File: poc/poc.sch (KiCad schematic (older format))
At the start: 47 parts

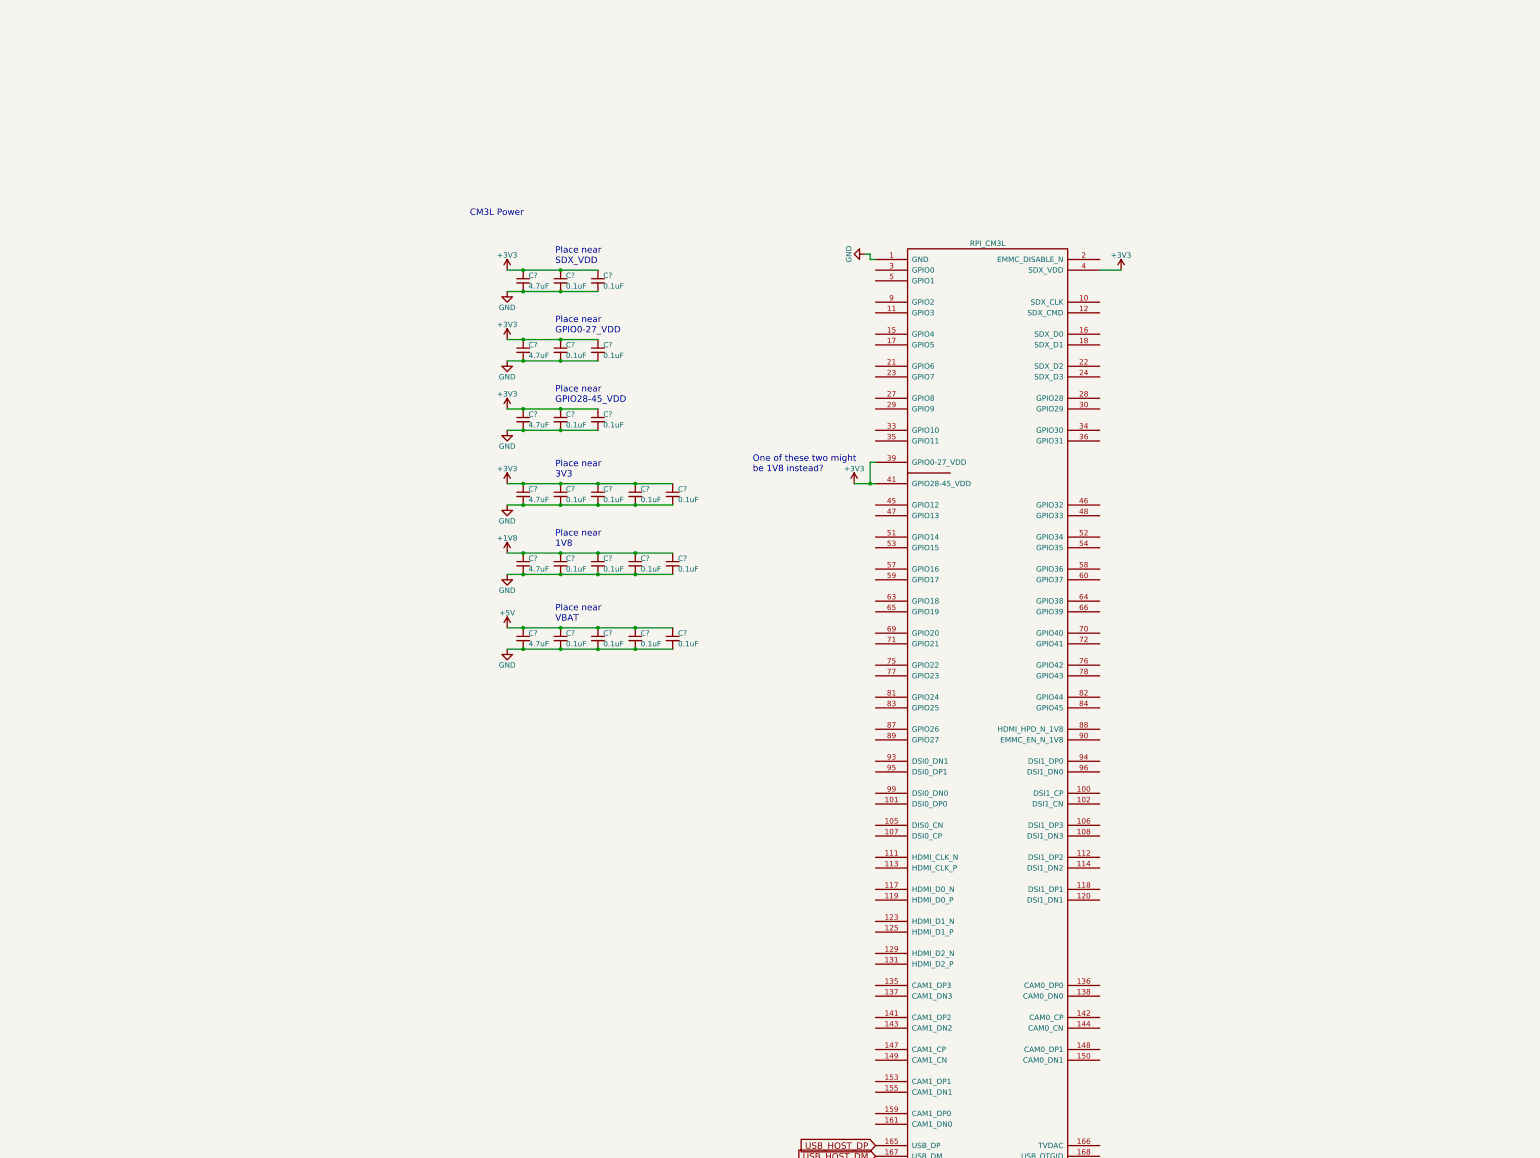
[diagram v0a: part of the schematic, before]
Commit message: Done with power layout for top cm3l
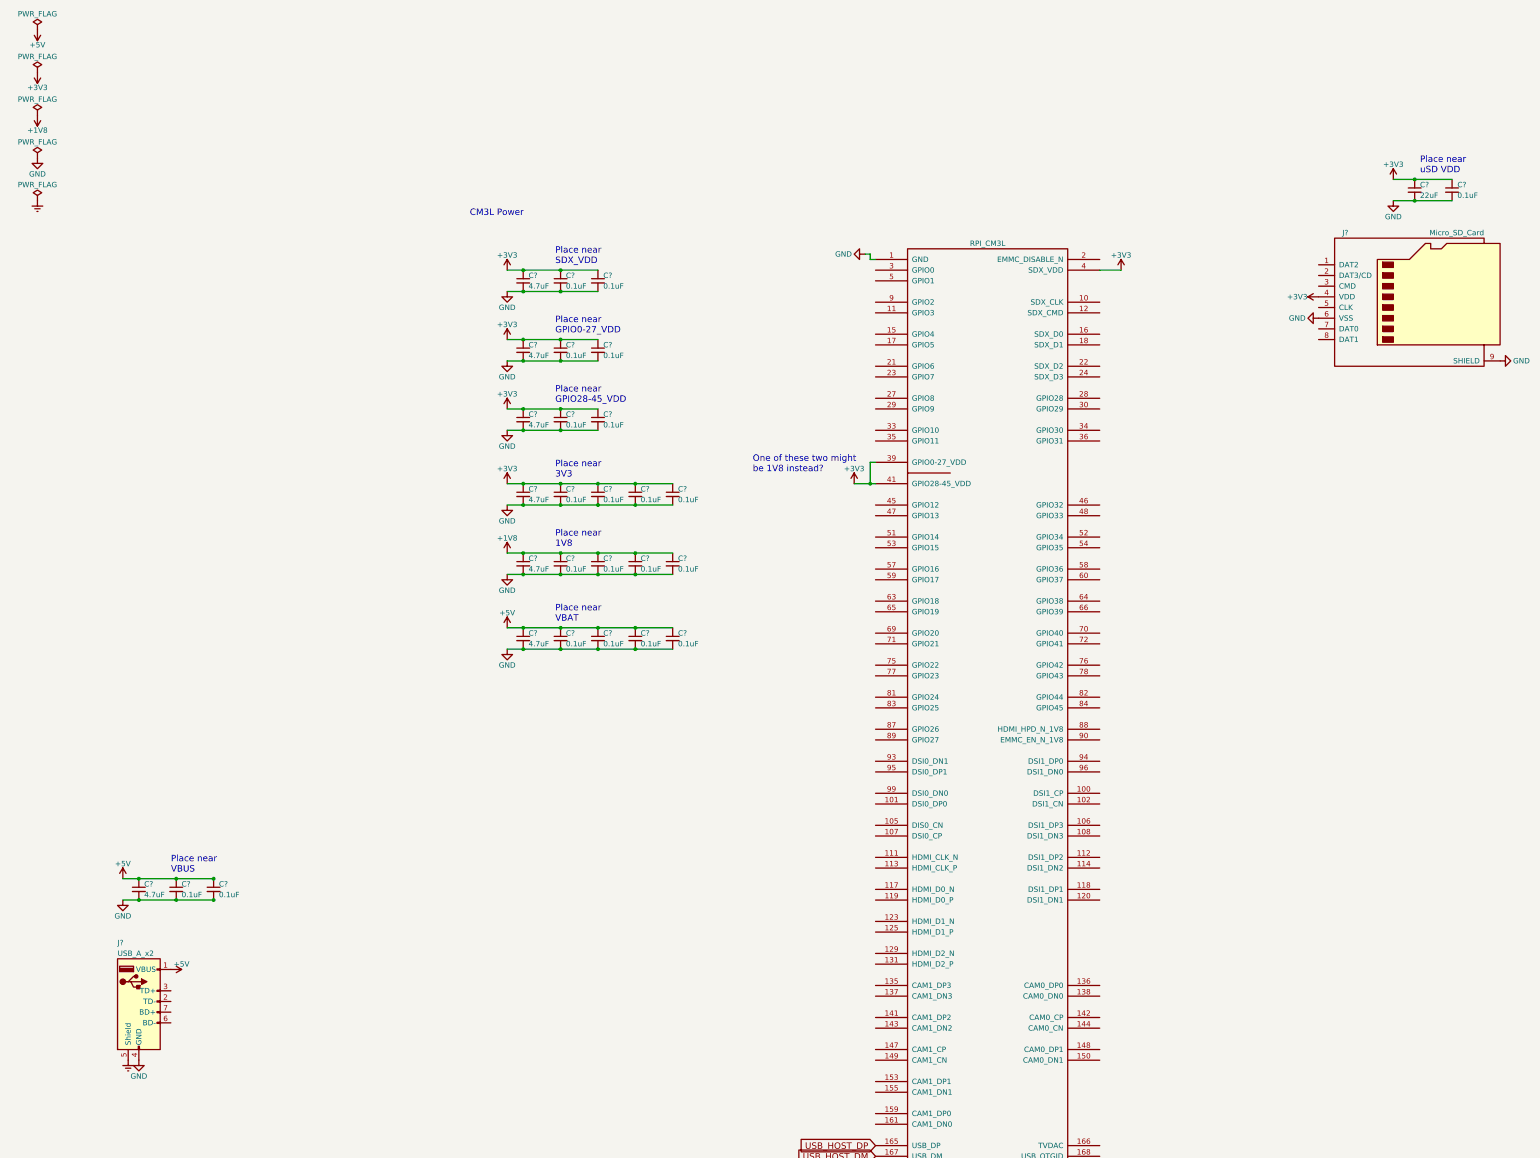
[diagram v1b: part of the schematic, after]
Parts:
- added C?: 4.7uF, symbol C_Small
- added C? (x3): 0.1uF, symbol C_Small
- added C?: 22uF, symbol C_Small
- added J?: USB_A_x2, symbol USB_A_x2
- added J?: Micro_SD_Card, symbol Micro_SD_Card
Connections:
- net +3V3: now also C?.1, C?.1, J?.4 (VDD)
- net +5V: now also C?.1, C?.1, C?.1, J?.1 (VBUS), J?.5 (VBUS)
- net GND: now also C?.2, C?.2, C?.2, C?.2, C?.2, J?.4 (GND), J?.6 (VSS), J?.8 (GND), J?.9 (SHIELD)
- new net Earth: J?.5 (VBUS)
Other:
- note added: "Place near\nVBUS"
- note added: "Place near\nuSD VDD"

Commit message: Move CM3L into hierarchical sheet
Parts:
- removed C? (x37): 0.1uF, symbol C_Small
- removed C? (x9): 4.7uF, symbol C_Small
- removed C?: 1.0uF, symbol C_Small
- removed C?: 22uF, symbol C_Small
- removed J?: USB_A_x2, symbol USB_A_x2
- removed J?: Micro_SD_Card, symbol Micro_SD_Card
- removed L? (x2): 120Ω @ 100MHz; 2.0A, symbol L_Core_Ferrite
- removed TopPi1: RPI_CM3L, symbol RPI_CM3L
- removed U?: LAN9512, MODULE, symbol LAN9512
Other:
- note removed: "CM3L Power"
- note removed: "Ferrite Bead"
- note removed: "LAN9512 Power"
- note removed: "One of these two might\nbe 1V8 instead?"
- note removed: "Place near\n1V8"
- note removed: "Place near\n3V3"
- note removed: "Place near\nGPIO0-27_VDD"
- note removed: "Place near\nGPIO28-45_VDD"
- note removed: "Place near\nSDX_VDD"
- note removed: "Place near\nVBAT"
- note removed: "Place near\nVBUS"
- note removed: "Place near\nVDD18CORE"
- note removed: "Place near\nVDD33A"
- note removed: "Place near\nVDD33IO"
- note removed: "Place near\nuSD VDD"

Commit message: Add one switch chip and power for things
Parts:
- added C? (x14): 0.1uF, symbol C_Small
- added C? (x2): 4.7uF, symbol C_Small
- added U?: SAM4E, MODULE, symbol SAM4E
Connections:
- net +3V3: now also C?.1, C?.1, C?.1, C?.1, C?.1, C?.1, C?.1, C?.1, U?.134 (VDDIO), U?.143 (VDDIO), U?.30 (VDDIO), U?.43 (VDDIO), U?.5 (VDDIN), U?.72 (VDDIO), U?.80 (VDDIO), U?.96 (VDDIO)
- net GND: now also C?.2, C?.2, C?.2, C?.2, C?.2, C?.2, C?.2, C?.2, C?.2, C?.2, C?.2, C?.2, C?.2, C?.2, C?.2, C?.2, U?.115 (GND), U?.135 (GND), U?.138 (GND), U?.44 (GND), U?.61 (GND), U?.8 (GND), U?.95 (GND)
- new net VDDCORE: C?.1, C?.1, C?.1, C?.1, C?.1, C?.1, C?.1, C?.1, U?.107 (VDDCORE), U?.123 (VDDCORE), U?.139 (VDDPLL), U?.29 (VDDCORE), U?.3 (VDDOUT), U?.33 (VDDCORE), U?.50 (VDDCORE), U?.81 (VDDCORE)
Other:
- note added: "Place near\nVDDCORE \n& VDDPLL"
- note added: "Place near\nVDDIO\n& VDDIN"

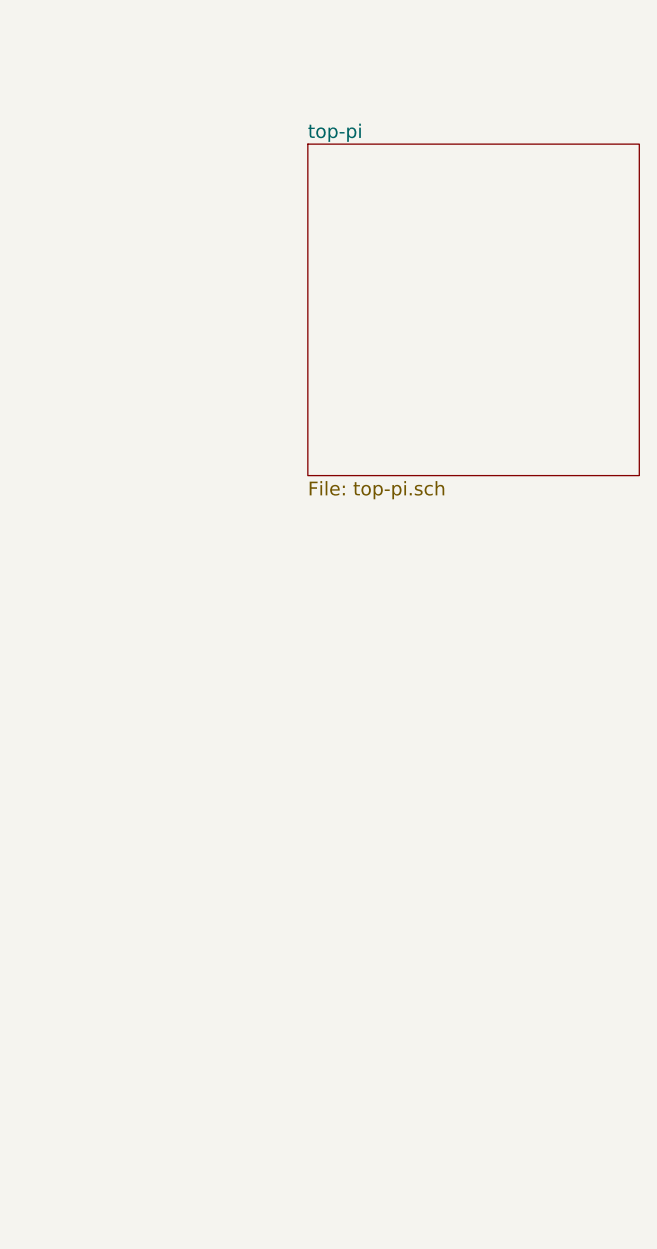
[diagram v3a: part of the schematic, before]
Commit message: Further organize pi schematics; power for each chip is done!
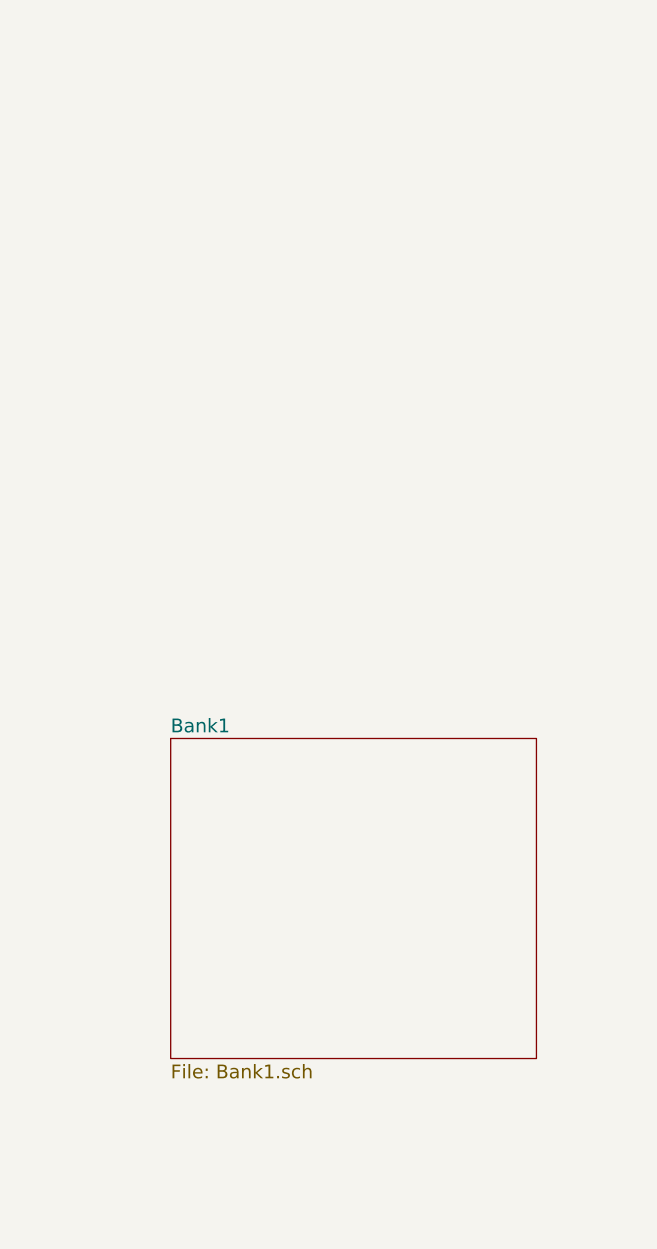
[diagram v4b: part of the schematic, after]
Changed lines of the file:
@@
 $Descr C 22000 17000
 encoding utf-8
-Sheet 1 3
+Sheet 1 4
 Title ""
 Date ""
@@
 	1    0    0    -1
 $EndComp
-$Sheet
-S 17850 1050 1450 1450
-U 598EEE5F
-F0 "top-pi" 60
-F1 "top-pi.sch" 60
-$EndSheet
 $Comp
 L SAM4E U?
@@
 F1 "switches.sch" 60
 $EndSheet
+$Sheet
+S 17250 3650 1600 1400
+U 5992D94E
+F0 "Bank1" 60
+F1 "Bank1.sch" 60
+$EndSheet
 $EndSCHEMATC

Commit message: Upgrade to newer kicad
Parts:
- C? (x16): symbol C_Small -> poc-rescue:C_Small
- U?: symbol SAM4E -> SAM4E:SAM4E
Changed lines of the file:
@@
-EESchema Schematic File Version 2
-LIBS:power
-LIBS:device
-LIBS:transistors
-LIBS:conn
-LIBS:linear
-LIBS:regul
-LIBS:74xx
-LIBS:cmos4000
-LIBS:adc-dac
-LIBS:memory
-LIBS:xilinx
-LIBS:microcontrollers
-LIBS:dsp
-LIBS:microchip
-LIBS:analog_switches
-LIBS:motorola
-LIBS:texas
-LIBS:intel
-LIBS:audio
-LIBS:interface
-LIBS:digital-audio
-LIBS:philips
-LIBS:display
-LIBS:cypress
-LIBS:siliconi
-LIBS:opto
-LIBS:atmel
-LIBS:contrib
-LIBS:valves
-LIBS:cm3l
-LIBS:LAN9512
-LIBS:usb_a_x2
-LIBS:CD74HC154
-LIBS:sc16is752
-LIBS:KSZ9897R
-LIBS:belfuse_gige
-LIBS:SAM4E
-LIBS:DP83867
-LIBS:ds75
+EESchema Schematic File Version 4
 LIBS:poc-cache
-EELAYER 25 0
+EELAYER 30 0
 EELAYER END
 $Descr C 22000 17000
@@
 $EndDescr
 $Comp
-L +5V #PWR01
+L power:+5V #PWR01
 U 1 1 59896F64
 P 800 700
@@
 $EndComp
 $Comp
-L GND #PWR02
+L power:GND #PWR02
 U 1 1 59897011
 P 800 1900
@@
 $EndComp
 $Comp
-L Earth #PWR03
+L power:Earth #PWR03
 U 1 1 598972A4
 P 800 2300
@@
 $EndComp
 $Comp
-L +3V3 #PWR04
+L power:+3V3 #PWR04
 U 1 1 5989782B
 P 800 1100
@@
 $EndComp
 $Comp
-L +1V8 #PWR05
+L power:+1V8 #PWR05
 U 1 1 59897F2C
 P 800 1500
@@
 $EndComp
 $Comp
-L PWR_FLAG #FLG06
+L power:PWR_FLAG #FLG06
 U 1 1 59898EBD
 P 800 700
@@
 $EndComp
 $Comp
-L PWR_FLAG #FLG07
+L power:PWR_FLAG #FLG07
 U 1 1 59898F71
 P 800 1100
@@
 $EndComp
 $Comp
-L PWR_FLAG #FLG08
+L power:PWR_FLAG #FLG08
 U 1 1 5989901E
 P 800 1500
@@
 $EndComp
 $Comp
-L PWR_FLAG #FLG09
+L power:PWR_FLAG #FLG09
 U 1 1 59899101
 P 800 1900
@@
 $EndComp
 $Comp
-L PWR_FLAG #FLG010
+L power:PWR_FLAG #FLG010
 U 1 1 59899286
 P 800 2300
@@
 $EndComp
 $Comp
-L +5V #PWR011
+L power:+5V #PWR011
 U 1 1 598CFAE4
 P 800 700
@@
 $EndComp
 $Comp
-L GND #PWR012
+L power:GND #PWR012
 U 1 1 598CFAE5
 P 800 1900
@@
 $EndComp
 $Comp
-L Earth #PWR013
+L power:Earth #PWR013
 U 1 1 598CFAE6
 P 800 2300
@@
 $EndComp
 $Comp
-L +3V3 #PWR014
+L power:+3V3 #PWR014
 U 1 1 598CFAE7
 P 800 1100
@@
 $EndComp
 $Comp
-L +1V8 #PWR015
+L power:+1V8 #PWR015
 U 1 1 598CFAE8
 P 800 1500
@@
 $EndComp
 $Comp
-L PWR_FLAG #FLG016
+L power:PWR_FLAG #FLG016
 U 1 1 598CFAE9
 P 800 700
@@
 $EndComp
 $Comp
-L PWR_FLAG #FLG017
+L power:PWR_FLAG #FLG017
 U 1 1 598CFAEA
 P 800 1100
@@
 $EndComp
 $Comp
-L PWR_FLAG #FLG018
+L power:PWR_FLAG #FLG018
 U 1 1 598CFAEB
 P 800 1500
@@
 $EndComp
 $Comp
-L PWR_FLAG #FLG019
+L power:PWR_FLAG #FLG019
 U 1 1 598CFAEC
 P 800 1900
@@
 $EndComp
 $Comp
-L PWR_FLAG #FLG020
+L power:PWR_FLAG #FLG020
 U 1 1 598CFAED
 P 800 2300
@@
 $EndComp
 $Comp
-L SAM4E U?
+L SAM4E:SAM4E U?
 U 1 1 59906DC8
 P 6900 8400
@@
 $EndComp
 $Comp
-L GND #PWR021
+L power:GND #PWR021
 U 1 1 59906F6C
 P 5850 10650
@@
 $EndComp
 $Comp
-L +3V3 #PWR022
+L power:+3V3 #PWR022
 U 1 1 59906F8C
 P 5550 10650
@@
 $EndComp
 $Comp
-L +3V3 #PWR023
+L power:+3V3 #PWR023
 U 1 1 59906FC0
 P 8050 10650
@@
 INT_REG
 $Comp
-L GND #PWR024
+L power:GND #PWR024
 U 1 1 5990729C
 P 3800 11850
@@
 $EndComp
 $Comp
-L C_Small C?
+L poc-rescue:C_Small C?
 U 1 1 599072AE
 P 4350 11750
@@
 $EndComp
 $Comp
-L C_Small C?
+L poc-rescue:C_Small C?
 U 1 1 5990730A
 P 4650 11750
@@
 $EndComp
 $Comp
-L C_Small C?
+L poc-rescue:C_Small C?
 U 1 1 59907382
 P 4950 11750
@@
 $EndComp
 $Comp
-L C_Small C?
+L poc-rescue:C_Small C?
 U 1 1 59907388
 P 5250 11750
@@
 $EndComp
 $Comp
-L C_Small C?
+L poc-rescue:C_Small C?
 U 1 1 599073D7
 P 5550 11750
@@
 $EndComp
 $Comp
-L C_Small C?
+L poc-rescue:C_Small C?
 U 1 1 599073DD
 P 5850 11750
@@
 $EndComp
 $Comp
-L C_Small C?
+L poc-rescue:C_Small C?
 U 1 1 599073F1
 P 6150 11750
@@
 $EndComp
 $Comp
-L C_Small C?
+L poc-rescue:C_Small C?
 U 1 1 5990749D
 P 4050 11750
@@
 $EndComp
 Wire Wire Line
-	3800 11650 6150 11650
-Wire Wire Line
-	3800 11850 6150 11850
+	3800 11650 4050 11650
+Wire Wire Line
+	3800 11850 4050 11850
 Connection ~ 4050 11650
 Connection ~ 4350 11650
@@
 Place near\nVDDCORE \n& VDDPLL
 $Comp
-L GND #PWR025
+L power:GND #PWR025
 U 1 1 5990793F
 P 3750 12550
@@
 $EndComp
 $Comp
-L C_Small C?
+L poc-rescue:C_Small C?
 U 1 1 59907945
 P 4300 12450
@@
 $EndComp
 $Comp
-L C_Small C?
+L poc-rescue:C_Small C?
 U 1 1 5990794B
 P 4600 12450
@@
 $EndComp
 $Comp
-L C_Small C?
+L poc-rescue:C_Small C?
 U 1 1 59907951
 P 4900 12450
@@
 $EndComp
 $Comp
-L C_Small C?
+L poc-rescue:C_Small C?
 U 1 1 59907957
 P 5200 12450
@@
 $EndComp
 $Comp
-L C_Small C?
+L poc-rescue:C_Small C?
 U 1 1 5990795D
 P 5500 12450
@@
 $EndComp
 $Comp
-L C_Small C?
+L poc-rescue:C_Small C?
 U 1 1 59907963
 P 5800 12450
@@
 $EndComp
 $Comp
-L C_Small C?
+L poc-rescue:C_Small C?
 U 1 1 59907969
 P 6100 12450
@@
 $EndComp
 $Comp
-L C_Small C?
+L poc-rescue:C_Small C?
 U 1 1 5990796F
 P 4000 12450
@@
 $EndComp
 Wire Wire Line
-	3750 12350 6100 12350
-Wire Wire Line
-	3750 12550 6100 12550
+	3750 12350 4000 12350
+Wire Wire Line
+	3750 12550 4000 12550
 Connection ~ 4000 12350
 Connection ~ 4300 12350
@@
 Place near\nVDDIO\n& VDDIN
 $Comp
-L +3V3 #PWR026
+L power:+3V3 #PWR026
 U 1 1 59907C36
 P 3750 12350
@@
 F1 "Bank1.sch" 60
 $EndSheet
+Wire Wire Line
+	4050 11650 4350 11650
+Wire Wire Line
+	4350 11650 4650 11650
+Wire Wire Line
+	4650 11650 4950 11650
+Wire Wire Line
+	4950 11650 5250 11650
+Wire Wire Line
+	5250 11650 5550 11650
+Wire Wire Line
+	5550 11650 5850 11650
+Wire Wire Line
+	5850 11650 6150 11650
+Wire Wire Line
+	5850 11850 6150 11850
+Wire Wire Line
+	5550 11850 5850 11850
+Wire Wire Line
+	5250 11850 5550 11850
+Wire Wire Line
+	4950 11850 5250 11850
+Wire Wire Line
+	4650 11850 4950 11850
+Wire Wire Line
+	4350 11850 4650 11850
+Wire Wire Line
+	4050 11850 4350 11850
+Wire Wire Line
+	4000 12350 4300 12350
+Wire Wire Line
+	4300 12350 4600 12350
+Wire Wire Line
+	4600 12350 4900 12350
+Wire Wire Line
+	4900 12350 5200 12350
+Wire Wire Line
+	5200 12350 5500 12350
+Wire Wire Line
+	5500 12350 5800 12350
+Wire Wire Line
+	5800 12350 6100 12350
+Wire Wire Line
+	5800 12550 6100 12550
+Wire Wire Line
+	5500 12550 5800 12550
+Wire Wire Line
+	5200 12550 5500 12550
+Wire Wire Line
+	4900 12550 5200 12550
+Wire Wire Line
+	4600 12550 4900 12550
+Wire Wire Line
+	4300 12550 4600 12550
+Wire Wire Line
+	4000 12550 4300 12550
 $EndSCHEMATC
